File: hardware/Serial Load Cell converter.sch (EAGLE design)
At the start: 51 parts, among them J1 AVR_PRG, J3 RJ11, U1 HX711, U2 ATMEGA328, U3 TMP102, U4 FT232RLSSOP, U5 MIC52055-5V, X1 USBSMD, Y2 16MHz

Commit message: Fixing file locations.
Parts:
- removed S1: Reset, SparkFun-Electromechanical:TAC_SWITCHSMD
- removed U4: FT232RLSSOP, SparkFun-DigitalIC:FT232RLSSOP
- added C2, C5: 47pF, SparkFun-Capacitors:47PF-50V-5%(0603)
- added R1, R6: 27, SparkFun-Resistors:27OHM1/10W1%(0603)
- added S2: Reset, SparkFun-Electromechanical:SWITCH-MOMENTARY-2SMD
- added U6: FTS31X, SparkFun-DigitalIC:FT231XS
- D2: value RED -> BLUE; device SparkFun-LED:LED-RED1206 -> SparkFun-LED:LED-BLUE1206
- FRAME1: DESIGNER (none) -> N. Seidle; VERSION (none) -> 01
- R10, R3, R4: device SparkFun-Resistors:100OHM1/10W1%(0603) -> SparkFun-Resistors:100OHM-1/10W-1%(0603)
- R13, R15: value 1k -> 1K; device SparkFun-Resistors:1KOHM1/10W1%(0603) -> SparkFun-Resistors:1KOHM-1/10W-1%(0603)
- R2: value 10k -> 10K; device SparkFun-Resistors:10KOHM1/10W1%(0603)0603 -> SparkFun-Resistors:10KOHM-1/10W-1%(0603)0603
- R7: device SparkFun-Resistors:10KOHM1/10W1%(0603)0603 -> SparkFun-Resistors:10KOHM-1/10W-1%(0603)0603
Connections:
- removed net USB_D+: U4.USBDP, X1.D+
- removed net USB_D-: U4.USBDM, X1.D-
- new net N$13: R1.2, U6.USBDP
- new net N$4: C5.1, R6.1, X1.D-
- new net N$7: C2.1, R1.1, X1.D+
- new net N$8: R6.2, U6.USBDM
- net 3.3V: now also U6.!RESET, U6.3V3OUT; no longer U4.3V3OUT
- net 5V: now also U6.VCC, U6.VCCIO; no longer U4.VCC, U4.VCCIO
- net DTR: now also U6.!DTR; no longer U4.DTR
- net GND: now also C2.2, C5.2, S2.1, U6.GND@16, U6.GND@6; no longer S1.3, S1.4, U4.AGND, U4.GND18, U4.GND21, U4.GND7, U4.TEST
- net RST: now also S2.2; no longer S1.1
- net RXD: now also U6.TXD; no longer U4.TXD
- net RXLED: now also LED6.C, U6.CBUS1; no longer LED7.C, U4.RXLED
- net TXD: now also U6.RXD; no longer U4.RXD
- net TXLED: now also LED7.C, U6.CBUS2; no longer LED6.C, U4.TXLED
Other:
- note added: "Low noise regulator"
- note added: "Not sure about this v-reg. 5V from USB may not be enough to clean up AVDD."
- note added: "Temperature Compensation"
- note removed: "AVDD = VBG(R1+R2)/R1"
- note removed: "N. Seidle"
- note removed: "Temperature"
- note removed: "USB - Serial"
- note removed: "v01"
- moved on the sheet: C10, C7, C8, C9, F1, J3, JP2, JP3, R13, R15, R3, R4

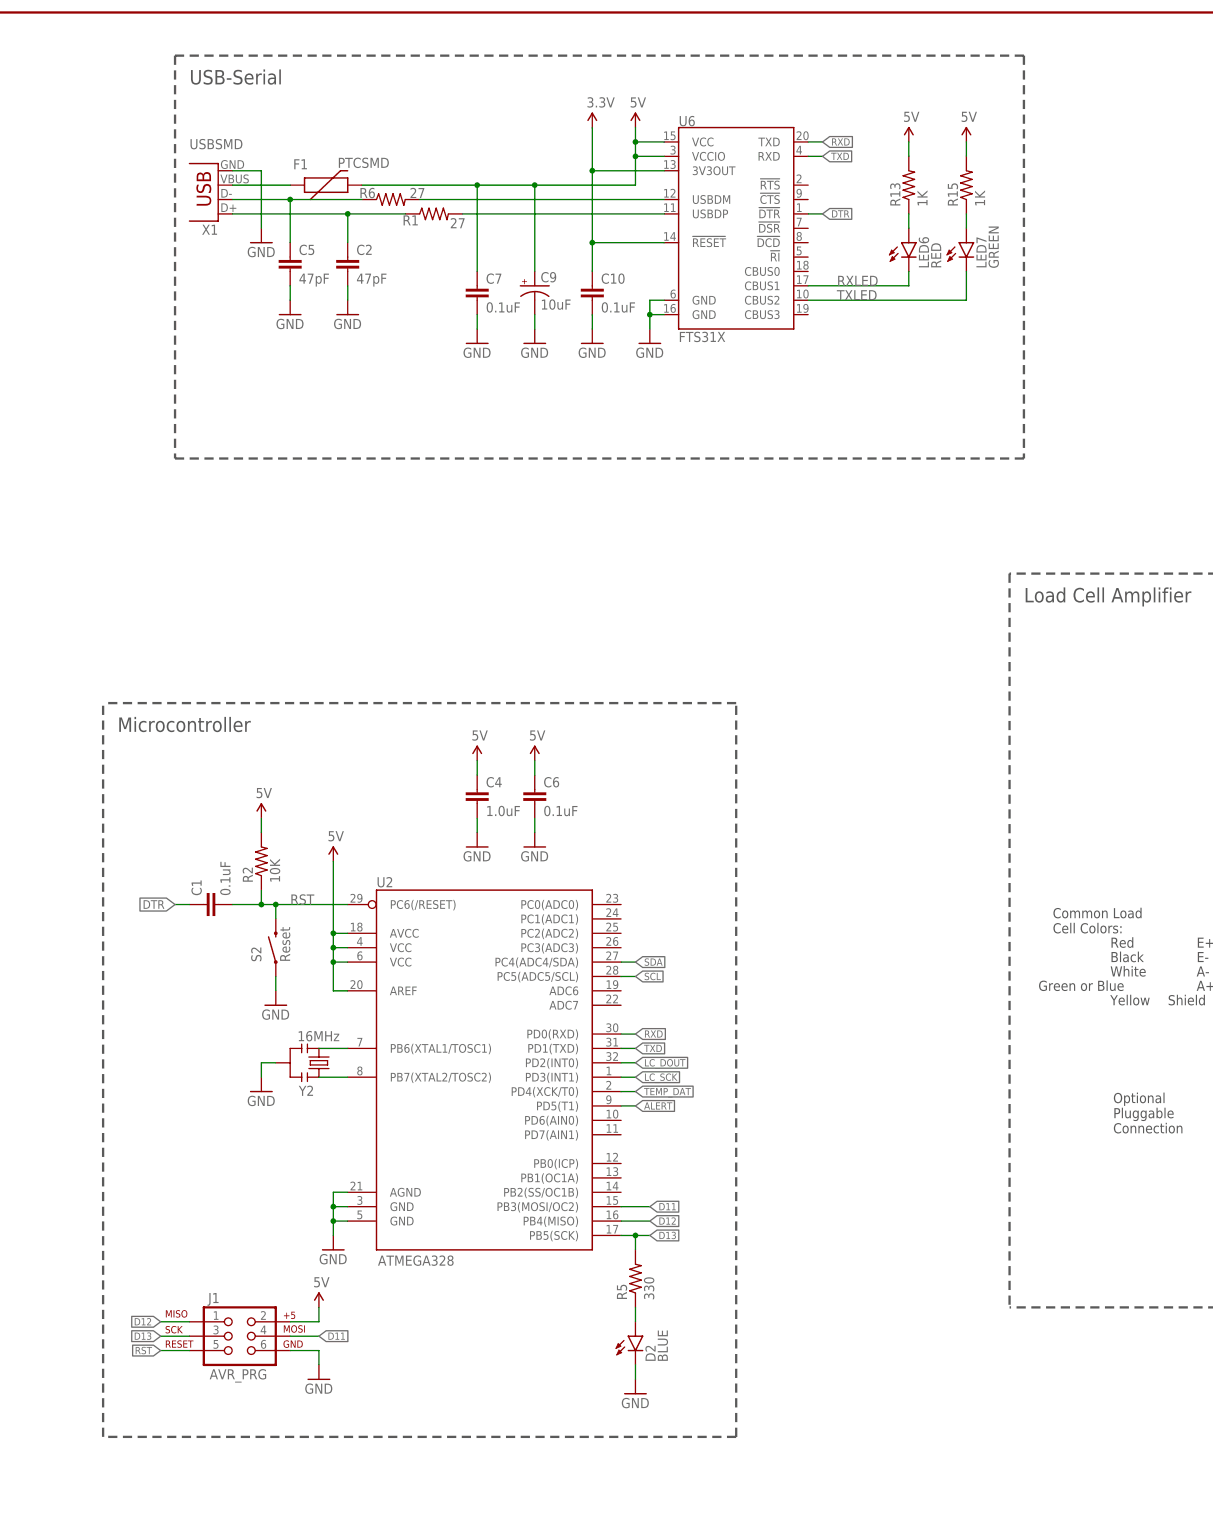
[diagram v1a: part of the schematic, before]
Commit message: Added external serial connection.
Can be used to emergency reset the serial interface back to 9600bps.
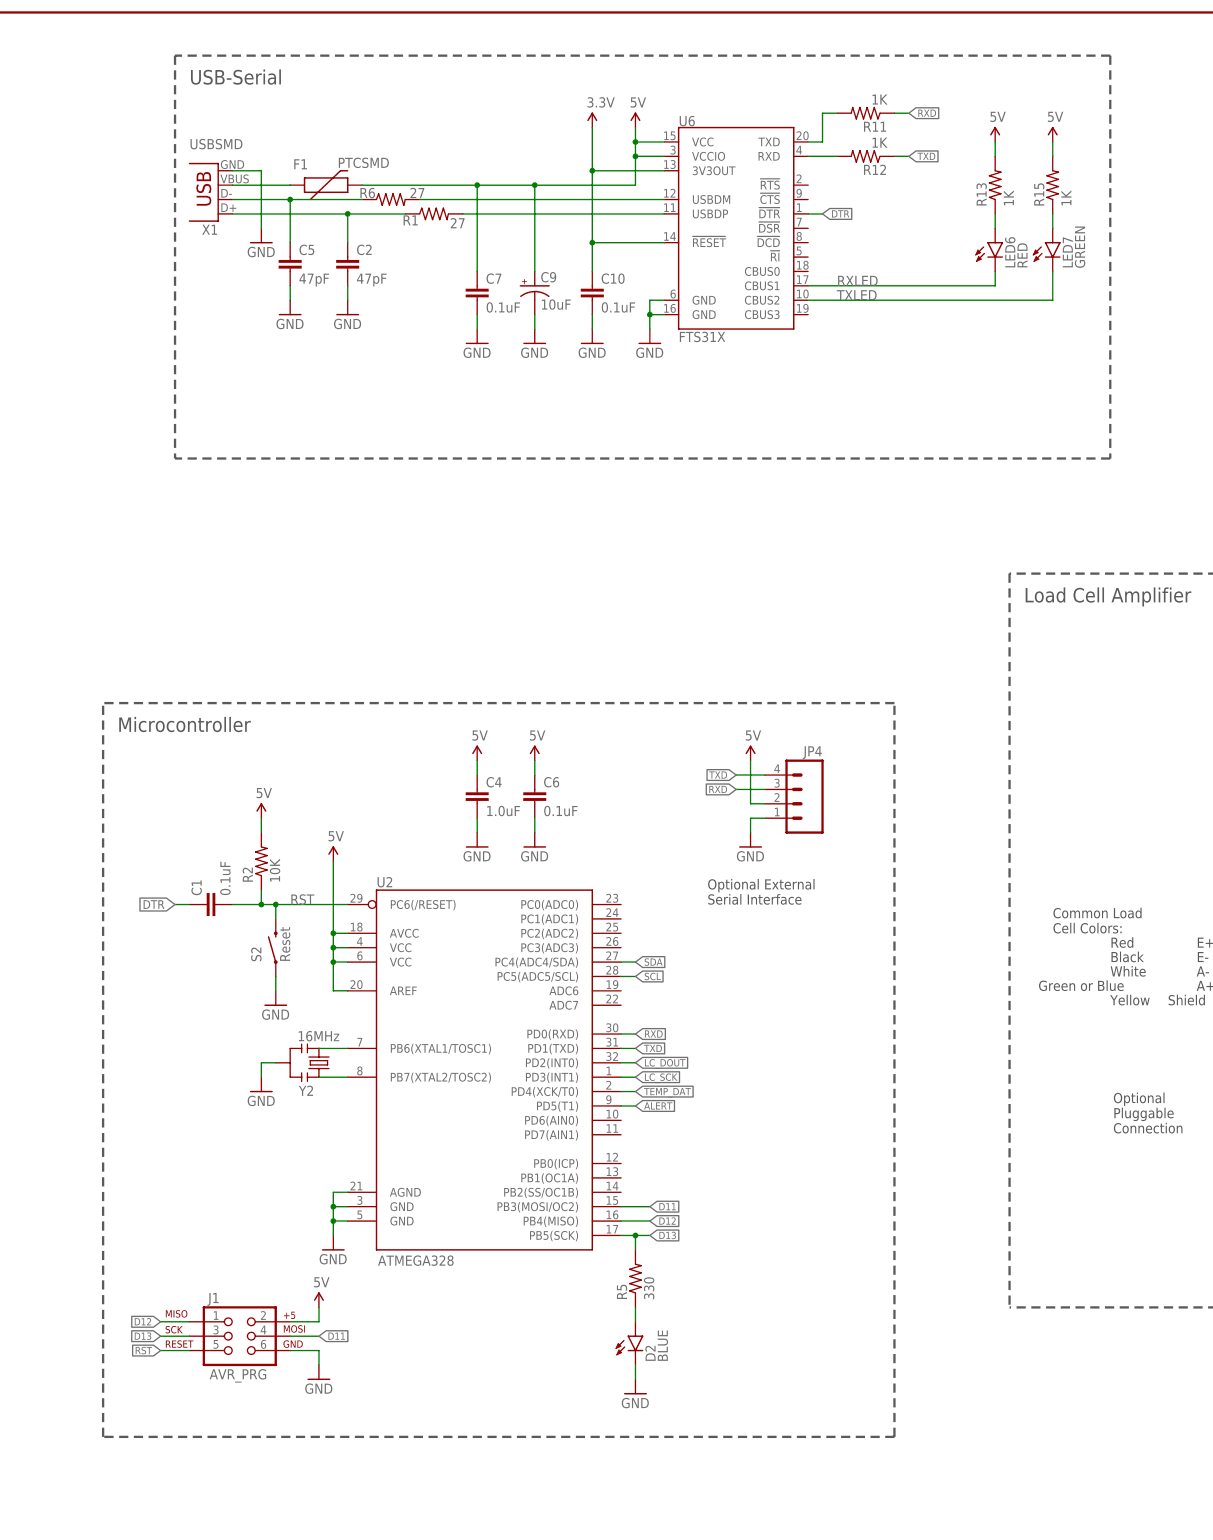
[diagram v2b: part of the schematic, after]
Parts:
- added JP4: (no value), SparkFun-Connectors:M04PTH
- added R11, R12: 1K, SparkFun-Resistors:1KOHM-1/10W-1%(0603)
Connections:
- new net N$14: R12.2, U6.RXD
- new net N$16: R11.2, U6.TXD
- net 5V: now also JP4.2
- net GND: now also JP4.1
- net RXD: now also JP4.3, R11.1; no longer U6.TXD
- net TXD: now also JP4.4, R12.1; no longer U6.RXD
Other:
- note added: "Optional External Serial Interface"
- moved on the sheet: LED6, LED7, R13, R15
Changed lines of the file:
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@@
 <part name="GND10" library="SparkFun" deviceset="GND" device=""/>
 <part name="GND12" library="SparkFun" deviceset="GND" device=""/>
+<part name="JP4" library="SparkFun-Connectors" deviceset="M04" device="PTH"/>
+<part name="U$10" library="SparkFun" deviceset="5V" device=""/>
+<part name="GND13" library="SparkFun" deviceset="GND" device=""/>
+<part name="R11" library="SparkFun-Resistors" deviceset="1KOHM-1/10W-1%(0603)" device="" value="1K"/>
+<part name="R12" library="SparkFun-Resistors" deviceset="1KOHM-1/10W-1%(0603)" device="" value="1K"/>
 </parts>
 <sheets>
 <sheet>
 <plain>
-<wire x1="190.5" y1="271.78" x2="40.64" y2="271.78" width="0.4064" layer="97" style="shortdash"/>
-<wire x1="190.5" y1="200.66" x2="40.64" y2="200.66" width="0.4064" layer="97" style="shortdash"/>
+<wire x1="205.74" y1="271.78" x2="40.64" y2="271.78" width="0.4064" layer="97" style="shortdash"/>
+<wire x1="205.74" y1="200.66" x2="40.64" y2="200.66" width="0.4064" layer="97" style="shortdash"/>
 <wire x1="40.64" y1="271.78" x2="40.64" y2="200.66" width="0.4064" layer="97" style="shortdash"/>
-<wire x1="190.5" y1="271.78" x2="190.5" y2="200.66" width="0.4064" layer="97" style="shortdash"/>
+<wire x1="205.74" y1="271.78" x2="205.74" y2="200.66" width="0.4064" layer="97" style="shortdash"/>
 <wire x1="27.94" y1="27.94" x2="27.94" y2="157.48" width="0.4064" layer="97" style="shortdash"/>
-<wire x1="139.7" y1="157.48" x2="27.94" y2="157.48" width="0.4064" layer="97" style="shortdash"/>
-<wire x1="139.7" y1="27.94" x2="27.94" y2="27.94" width="0.4064" layer="97" style="shortdash"/>
-<wire x1="139.7" y1="27.94" x2="139.7" y2="157.48" width="0.4064" layer="97" style="shortdash"/>
+<wire x1="167.64" y1="157.48" x2="27.94" y2="157.48" width="0.4064" layer="97" style="shortdash"/>
+<wire x1="167.64" y1="27.94" x2="27.94" y2="27.94" width="0.4064" layer="97" style="shortdash"/>
+<wire x1="167.64" y1="27.94" x2="167.64" y2="157.48" width="0.4064" layer="97" style="shortdash"/>
 <text x="30.48" y="152.4" size="2.54" layer="97">Microcontroller</text>
 <text x="43.18" y="266.7" size="2.54" layer="97">USB-Serial</text>
@@
 <text x="241.3" y="182.88" size="1.778" layer="91">Not sure about this v-reg. 5V from USB may not be enough to clean up AVDD.</text>
 <text x="289.56" y="137.16" size="1.778" layer="97">Low noise regulator</text>
+<text x="134.62" y="121.92" size="1.778" layer="97">Optional External
+Serial Interface</text>
 </plain>
 <instances>
@@
 <instance part="GND21" gate="1" x="93.98" y="220.98"/>
 <instance part="GND22" gate="1" x="104.14" y="220.98"/>
-<instance part="LED6" gate="G$1" x="170.18" y="238.76"/>
-<instance part="LED7" gate="G$1" x="180.34" y="238.76"/>
-<instance part="U$1" gate="G$1" x="170.18" y="256.54"/>
+<instance part="LED6" gate="G$1" x="185.42" y="238.76"/>
+<instance part="LED7" gate="G$1" x="195.58" y="238.76"/>
+<instance part="U$1" gate="G$1" x="185.42" y="256.54"/>
 <instance part="U$3" gate="G$1" x="121.92" y="259.08"/>
-<instance part="U$4" gate="G$1" x="180.34" y="256.54"/>
-<instance part="R13" gate="G$1" x="170.18" y="248.92" rot="R90"/>
-<instance part="R15" gate="G$1" x="180.34" y="248.92" rot="R90"/>
+<instance part="U$4" gate="G$1" x="195.58" y="256.54"/>
+<instance part="R13" gate="G$1" x="185.42" y="248.92" rot="R90"/>
+<instance part="R15" gate="G$1" x="195.58" y="248.92" rot="R90"/>
 <instance part="FRAME1" gate="G$1" x="0" y="0" smashed="yes">
 <attribute name="DESIGNER" x="0" y="0" size="1.778" layer="96" display="off"/>
@@
 <instance part="GND10" gate="1" x="60.96" y="226.06"/>
 <instance part="GND12" gate="1" x="71.12" y="226.06"/>
+<instance part="JP4" gate="G$1" x="149.86" y="139.7" rot="MR0"/>
+<instance part="U$10" gate="G$1" x="142.24" y="147.32"/>
+<instance part="GND13" gate="1" x="142.24" y="132.08"/>
+<instance part="R11" gate="G$1" x="162.56" y="261.62" rot="R180"/>
+<instance part="R12" gate="G$1" x="162.56" y="254" rot="R180"/>
 </instances>
 <busses>
@@
 <wire x1="71.12" y1="228.6" x2="71.12" y2="231.14" width="0.1524" layer="91"/>
 </segment>
+<segment>
+<pinref part="JP4" gate="G$1" pin="1"/>
+<wire x1="144.78" y1="137.16" x2="142.24" y2="137.16" width="0.1524" layer="91"/>
+<wire x1="142.24" y1="137.16" x2="142.24" y2="134.62" width="0.1524" layer="91"/>
+<pinref part="GND13" gate="1" pin="GND"/>
+</segment>
 </net>
 <net name="RST" class="0">
@@
 </segment>
 <segment>
-<wire x1="152.4" y1="256.54" x2="154.94" y2="256.54" width="0.1524" layer="91"/>
-<label x="154.94" y="256.54" size="1.27" layer="95" xref="yes"/>
-<pinref part="U6" gate="G$1" pin="TXD"/>
+<label x="170.18" y="261.62" size="1.27" layer="95" xref="yes"/>
+<pinref part="R11" gate="G$1" pin="1"/>
+<wire x1="167.64" y1="261.62" x2="170.18" y2="261.62" width="0.1524" layer="91"/>
+</segment>
+<segment>
+<pinref part="JP4" gate="G$1" pin="3"/>
+<wire x1="144.78" y1="142.24" x2="139.7" y2="142.24" width="0.1524" layer="91"/>
+<label x="139.7" y="142.24" size="1.27" layer="95" rot="R180" xref="yes"/>
 </segment>
 </net>
@@
 </segment>
 <segment>
-<wire x1="152.4" y1="254" x2="154.94" y2="254" width="0.1524" layer="91"/>
-<label x="154.94" y="254" size="1.27" layer="95" xref="yes"/>
-<pinref part="U6" gate="G$1" pin="RXD"/>
+<label x="170.18" y="254" size="1.27" layer="95" xref="yes"/>
+<wire x1="167.64" y1="254" x2="170.18" y2="254" width="0.1524" layer="91"/>
+<pinref part="R12" gate="G$1" pin="1"/>
+</segment>
+<segment>
+<pinref part="JP4" gate="G$1" pin="4"/>
+<wire x1="144.78" y1="144.78" x2="139.7" y2="144.78" width="0.1524" layer="91"/>
+<label x="139.7" y="144.78" size="1.27" layer="95" rot="R180" xref="yes"/>
 </segment>
 </net>
@@
 <net name="RXLED" class="0">
 <segment>
-<wire x1="152.4" y1="231.14" x2="170.18" y2="231.14" width="0.1524" layer="91"/>
-<wire x1="170.18" y1="231.14" x2="170.18" y2="233.68" width="0.1524" layer="91"/>
+<wire x1="152.4" y1="231.14" x2="185.42" y2="231.14" width="0.1524" layer="91"/>
+<wire x1="185.42" y1="231.14" x2="185.42" y2="233.68" width="0.1524" layer="91"/>
 <label x="157.48" y="231.14" size="1.778" layer="95"/>
 <pinref part="LED6" gate="G$1" pin="C"/>
@@
 <net name="TXLED" class="0">
 <segment>
-<wire x1="152.4" y1="228.6" x2="180.34" y2="228.6" width="0.1524" layer="91"/>
-<wire x1="180.34" y1="228.6" x2="180.34" y2="233.68" width="0.1524" layer="91"/>
+<wire x1="152.4" y1="228.6" x2="195.58" y2="228.6" width="0.1524" layer="91"/>
+<wire x1="195.58" y1="228.6" x2="195.58" y2="233.68" width="0.1524" layer="91"/>
 <label x="157.48" y="228.6" size="1.778" layer="95"/>
 <pinref part="LED7" gate="G$1" pin="C"/>
@@
 <net name="N$5" class="0">
 <segment>
-<wire x1="170.18" y1="243.84" x2="170.18" y2="241.3" width="0.1524" layer="91"/>
+<wire x1="185.42" y1="243.84" x2="185.42" y2="241.3" width="0.1524" layer="91"/>
 <pinref part="LED6" gate="G$1" pin="A"/>
 <pinref part="R13" gate="G$1" pin="1"/>
@@
 <net name="N$6" class="0">
 <segment>
-<wire x1="180.34" y1="243.84" x2="180.34" y2="241.3" width="0.1524" layer="91"/>
+<wire x1="195.58" y1="243.84" x2="195.58" y2="241.3" width="0.1524" layer="91"/>
 <pinref part="LED7" gate="G$1" pin="A"/>
 <pinref part="R15" gate="G$1" pin="1"/>
@@
 </segment>
 <segment>
-<wire x1="170.18" y1="256.54" x2="170.18" y2="254" width="0.1524" layer="91"/>
+<wire x1="185.42" y1="256.54" x2="185.42" y2="254" width="0.1524" layer="91"/>
 <pinref part="U$1" gate="G$1" pin="5V"/>
 <pinref part="R13" gate="G$1" pin="2"/>
 </segment>
 <segment>
-<wire x1="180.34" y1="256.54" x2="180.34" y2="254" width="0.1524" layer="91"/>
+<wire x1="195.58" y1="256.54" x2="195.58" y2="254" width="0.1524" layer="91"/>
 <pinref part="U$4" gate="G$1" pin="5V"/>
 <pinref part="R15" gate="G$1" pin="2"/>
@@
 <pinref part="U$6" gate="G$1" pin="5V"/>
 </segment>
+<segment>
+<pinref part="JP4" gate="G$1" pin="2"/>
+<wire x1="144.78" y1="139.7" x2="142.24" y2="139.7" width="0.1524" layer="91"/>
+<wire x1="142.24" y1="139.7" x2="142.24" y2="147.32" width="0.1524" layer="91"/>
+<pinref part="U$10" gate="G$1" pin="5V"/>
+</segment>
 </net>
 <net name="LC_DOUT" class="0">
@@
 </segment>
 </net>
+<net name="N$14" class="0">
+<segment>
+<pinref part="R12" gate="G$1" pin="2"/>
+<wire x1="152.4" y1="254" x2="157.48" y2="254" width="0.1524" layer="91"/>
+<pinref part="U6" gate="G$1" pin="RXD"/>
+</segment>
+</net>
+<net name="N$16" class="0">
+<segment>
+<pinref part="R11" gate="G$1" pin="2"/>
+<wire x1="157.48" y1="261.62" x2="154.94" y2="261.62" width="0.1524" layer="91"/>
+<wire x1="154.94" y1="261.62" x2="154.94" y2="256.54" width="0.1524" layer="91"/>
+<wire x1="152.4" y1="256.54" x2="154.94" y2="256.54" width="0.1524" layer="91"/>
+<pinref part="U6" gate="G$1" pin="TXD"/>
+</segment>
+</net>

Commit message: First round of fixes from PLewis review
Fixed J1/J3 labels on schematic. Fixed LED colors to match standards.
Added test point for VCC. Improved layout around TMP102. Added measures.
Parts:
- removed LED6: RED, SparkFun-LED:LED-RED1206
- removed LED7: GREEN, SparkFun-LED:LED-GREENLARGE
- added D1: YELLOW, SparkFun-LED:LED-YELLOWLARGE
- added D3: BLUE, SparkFun-LED:LED-BLUE1206
- D2: value BLUE -> GREEN; device SparkFun-LED:LED-BLUE1206 -> SparkFun-LED:LED-GREENLARGE
- renumbered J1 to JP5, J3 to JP6, X1 to JP7
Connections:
- net GND: now also D3.C; no longer D2.C
- net N$2: now also D3.A; no longer D2.A
- net N$5: now also D1.A; no longer LED6.A
- net N$6: now also D2.A; no longer LED7.A
- net RXLED: now also D1.C; no longer LED6.C
- net TXLED: now also D2.C; no longer LED7.C
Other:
- moved on the sheet: C14, C15, C16, C18, D2, R10, U5

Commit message: Fixing issue #1
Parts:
- removed U2: ATMEGA328, SparkFun-DigitalIC:ATMEGA328_SMT
- added U4: ATMEGA328P_TQFP, SparkFun-DigitalIC:ATMEGA328P_TQFP
- FRAME1: VERSION 01 -> v01
- U6: value FTS31X -> FT231X
- Y2: value 16MHz -> 16MHZ
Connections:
- net 3.3V: now also U6.VCCIO
- net 5V: now also U4.AREF, U4.AVCC, U4.VCC@4, U4.VCC@6; no longer U2.AREF, U2.AVCC, U2.VCC@1, U2.VCC@2, U6.VCCIO
- net ALERT: now also U4.PD5(T1); no longer U2.PD5(T1)
- net D11: now also U4.PB3(MOSI/OC2); no longer U2.PB3(MOSI/OC2)
- net D12: now also U4.PB4(MISO); no longer U2.PB4(MISO)
- net D13: now also U4.PB5(SCK); no longer U2.PB5(SCK)
- net GND: now also U4.AGND, U4.GND@3, U4.GND@5; no longer U2.AGND, U2.GND@1, U2.GND@2
- net LC_DOUT: now also U4.PD2(INT0); no longer U2.PD2(INT0)
- net LC_SCK: now also U4.PD3(INT1); no longer U2.PD3(INT1)
- net N$1: now also U4.PB6(XTAL1/TOSC1); no longer U2.PB6(XTAL1/TOSC1)
- net N$3: now also U4.PB7(XTAL2/TOSC2); no longer U2.PB7(XTAL2/TOSC2)
- net RST: now also U4.PC6(/RESET); no longer U2.PC6(/RESET)
- net RXD: now also U4.PD0(RXD); no longer U2.PD0(RXD)
- net SCL: now also U4.PC5(ADC5/SCL); no longer U2.PC5(ADC5/SCL)
- net SDA: now also U4.PC4(ADC4/SDA); no longer U2.PC4(ADC4/SDA)
- net TEMP_DAT: now also U4.PD4(XCK/T0); no longer U2.PD4(XCK/T0)
- net TXD: now also U4.PD1(TXD); no longer U2.PD1(TXD)
